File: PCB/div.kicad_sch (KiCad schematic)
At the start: 27 parts, among them J2 Bus Gate Reset, Q4 BC557, U1 4024

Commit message: :hammer: Optimize schematic for PCB layout
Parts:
- D?: value rt -> ye
- J?: footprint Connector_PinHeader_2.54mm:PinHeader_2x08_P2.54mm_Vertical -> Connector_PinHeader_2.54mm:PinHeader_2x08_P2.54mm_Horizontal
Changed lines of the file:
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@@
       (effects (font (size 1.27 1.27)) (justify right))
     )
-    (property "Value" "rt" (at 107.315 36.195 90)
+    (property "Value" "ye" (at 107.315 36.195 90)
       (effects (font (size 1.27 1.27)) (justify right))
     )
@@
   (symbol (lib_id "Connector_Generic:Conn_02x08_Odd_Even") (at 40.64 181.61 180) (unit 1)
     (in_bom yes) (on_board yes) (dnp no) (fields_autoplaced)
-    (property "Reference" "J?" (at 39.37 166.4802 0)
-      (effects (font (size 1.27 1.27)))
-    )
-    (property "Value" "PWR" (at 39.37 169.0171 0)
-      (effects (font (size 1.27 1.27)))
-    )
-    (property "Footprint" "Connector_PinHeader_2.54mm:PinHeader_2x08_P2.54mm_Vertical" (at 40.64 181.61 0)
-      (effects (font (size 1.27 1.27)) hide)
-    )
+    (property "Reference" "J?" (at 39.37 167.1701 0)
+      (effects (font (size 1.27 1.27)))
+    )
+    (property "Value" "PWR" (at 39.37 169.0911 0)
+      (effects (font (size 1.27 1.27)))
+    )
+    (property "Footprint" "Connector_PinHeader_2.54mm:PinHeader_2x08_P2.54mm_Horizontal" (at 40.64 181.61 0)
+      (effects (font (size 1.27 1.27)) hide)
+    )

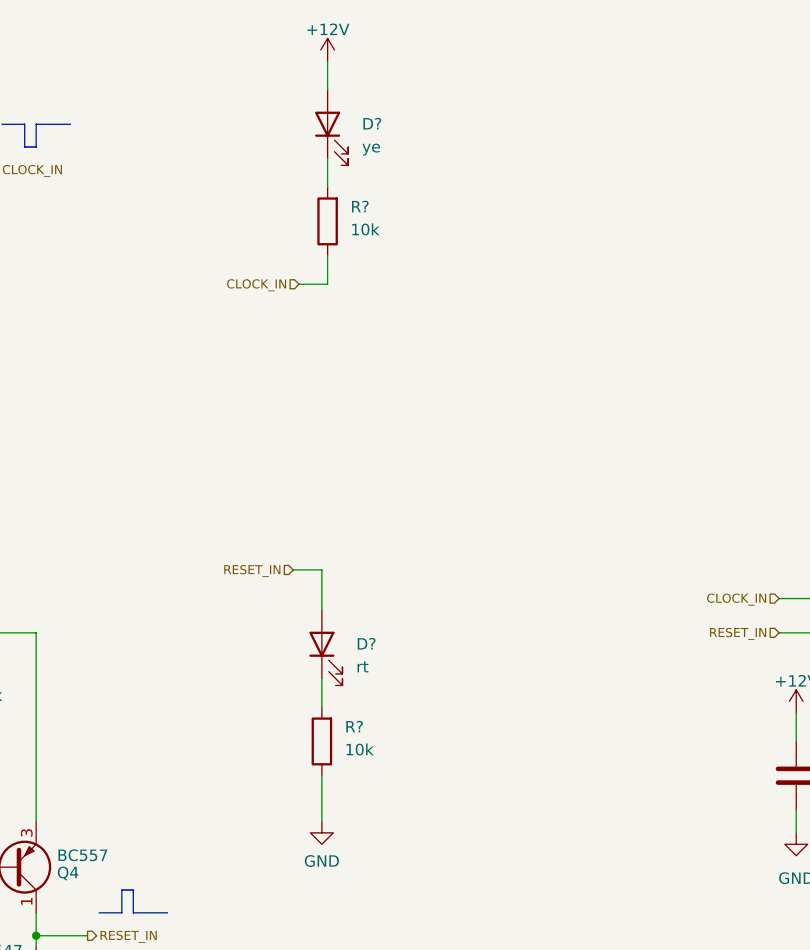
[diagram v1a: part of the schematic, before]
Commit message: :sparkles: Add jack LEDs to the schematic
Using clear jacks the LEDs can be put underneath them. The control
PCB can support both versions (LEDs separate or in jacks), so a
second (SMD) LED is added to the schematic.

Only one of these may be populated!
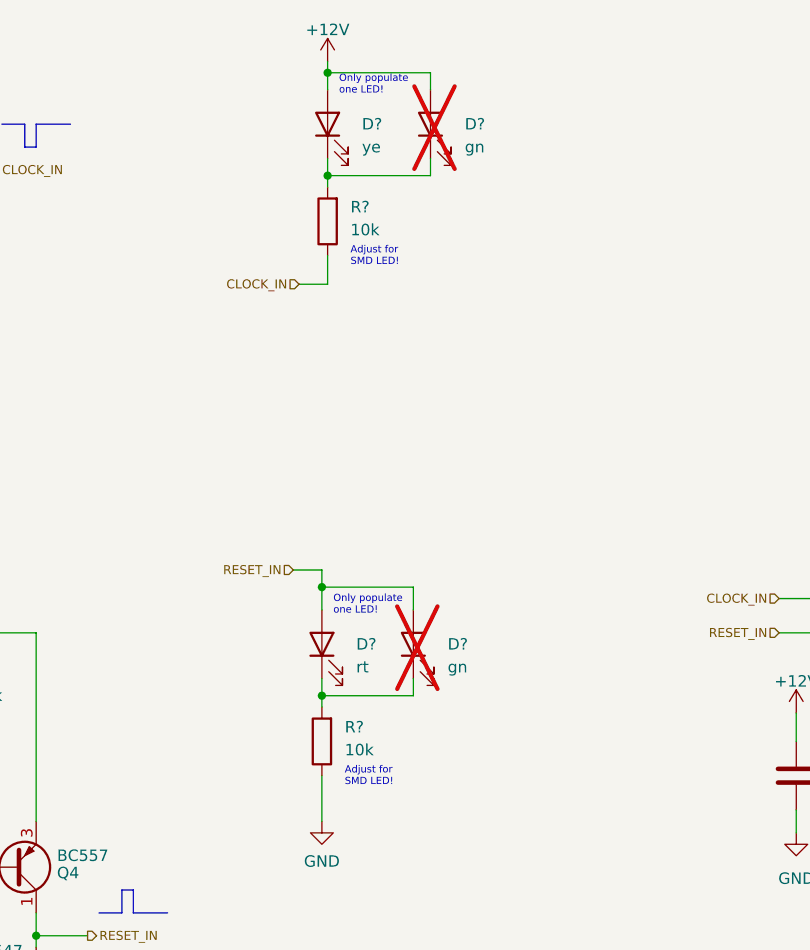
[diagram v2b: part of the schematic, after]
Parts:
- added D? (x2): gn, LED_SMD:LED_0805_2012Metric_Pad1.15x1.40mm_HandSolder, symbol Device:LED
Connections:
- net +12V: now also D?.2 (A)
- net RESET_IN: now also D?.2 (A)
- net at D?.1 (K), R?.2: now also D?.1 (K) (x2)
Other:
- note added: "Adjust for SMD LED!"
- note added: "Only populate one LED!"

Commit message: :hammer: Change power connector footprint in schematic
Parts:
- J?: footprint Connector_PinHeader_2.54mm:PinHeader_2x08_P2.54mm_Horizontal -> Connector_PinHeader_2.54mm:PinHeader_2x08_P2.54mm_Vertical
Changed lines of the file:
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@@
       (effects (font (size 1.27 1.27)))
     )
-    (property "Footprint" "Connector_PinHeader_2.54mm:PinHeader_2x08_P2.54mm_Horizontal" (at 40.64 181.61 0)
+    (property "Footprint" "Connector_PinHeader_2.54mm:PinHeader_2x08_P2.54mm_Vertical" (at 40.64 181.61 0)
       (effects (font (size 1.27 1.27)) hide)
     )

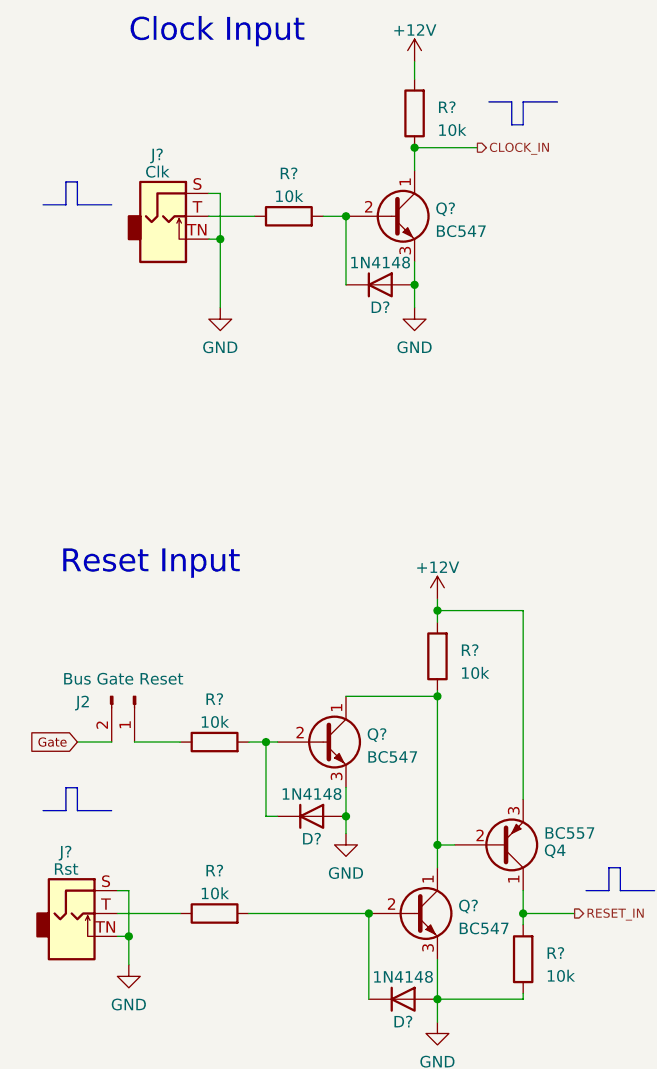
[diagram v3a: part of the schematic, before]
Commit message: :wrench: Increase input resistors to improve impedance
Set the input resistors to 100K to improve input impedance.
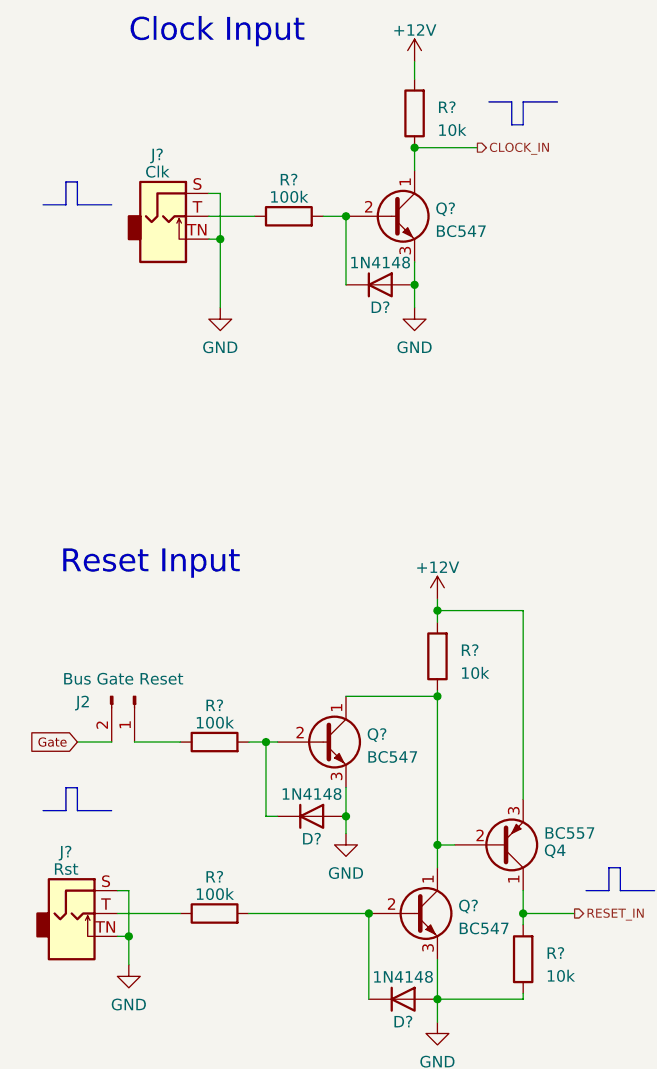
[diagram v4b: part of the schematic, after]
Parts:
- R? (x3): value 10k -> 100k
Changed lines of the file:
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@@
   (symbol (lib_id "Device:R") (at 36.83 104.775 90) (unit 1)
     (in_bom yes) (on_board yes) (dnp no) (fields_autoplaced)
-    (property "Reference" "R?" (at 36.83 100.0592 90)
-      (effects (font (size 1.27 1.27)))
-    )
-    (property "Value" "10k" (at 36.83 102.5961 90)
+    (property "Reference" "R?" (at 36.83 100.7491 90)
+      (effects (font (size 1.27 1.27)))
+    )
+    (property "Value" "100k" (at 36.83 102.6701 90)
       (effects (font (size 1.27 1.27)))
     )
@@
   (symbol (lib_id "Device:R") (at 36.83 123.825 90) (unit 1)
     (in_bom yes) (on_board yes) (dnp no) (fields_autoplaced)
-    (property "Reference" "R?" (at 36.83 119.1092 90)
-      (effects (font (size 1.27 1.27)))
-    )
-    (property "Value" "10k" (at 36.83 121.6461 90)
+    (property "Reference" "R?" (at 36.83 119.7991 90)
+      (effects (font (size 1.27 1.27)))
+    )
+    (property "Value" "100k" (at 36.83 121.7201 90)
       (effects (font (size 1.27 1.27)))
     )
@@
   (symbol (lib_id "Device:R") (at 45.085 46.355 90) (unit 1)
     (in_bom yes) (on_board yes) (dnp no) (fields_autoplaced)
-    (property "Reference" "R?" (at 45.085 41.6392 90)
-      (effects (font (size 1.27 1.27)))
-    )
-    (property "Value" "10k" (at 45.085 44.1761 90)
-      (effects (font (size 1.27 1.27)))
-    )
+    (property "Reference" "R?" (at 45.085 42.3291 90)
+      (effects (font (size 1.27 1.27)))
+    )
+    (property "Value" "100k" (at 45.085 44.2501 90)
+      (effects (font (size 1.27 1.27)))
+    )

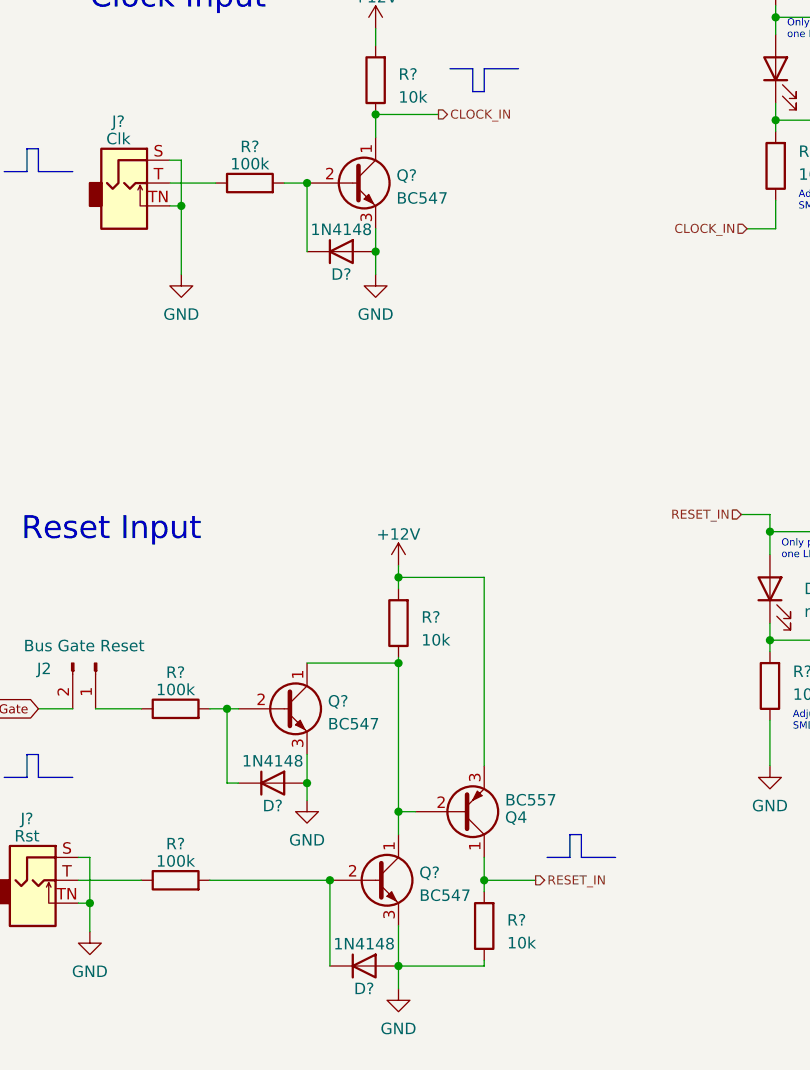
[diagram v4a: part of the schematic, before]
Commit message: :wrench: Change transistor footprint to handsolder version
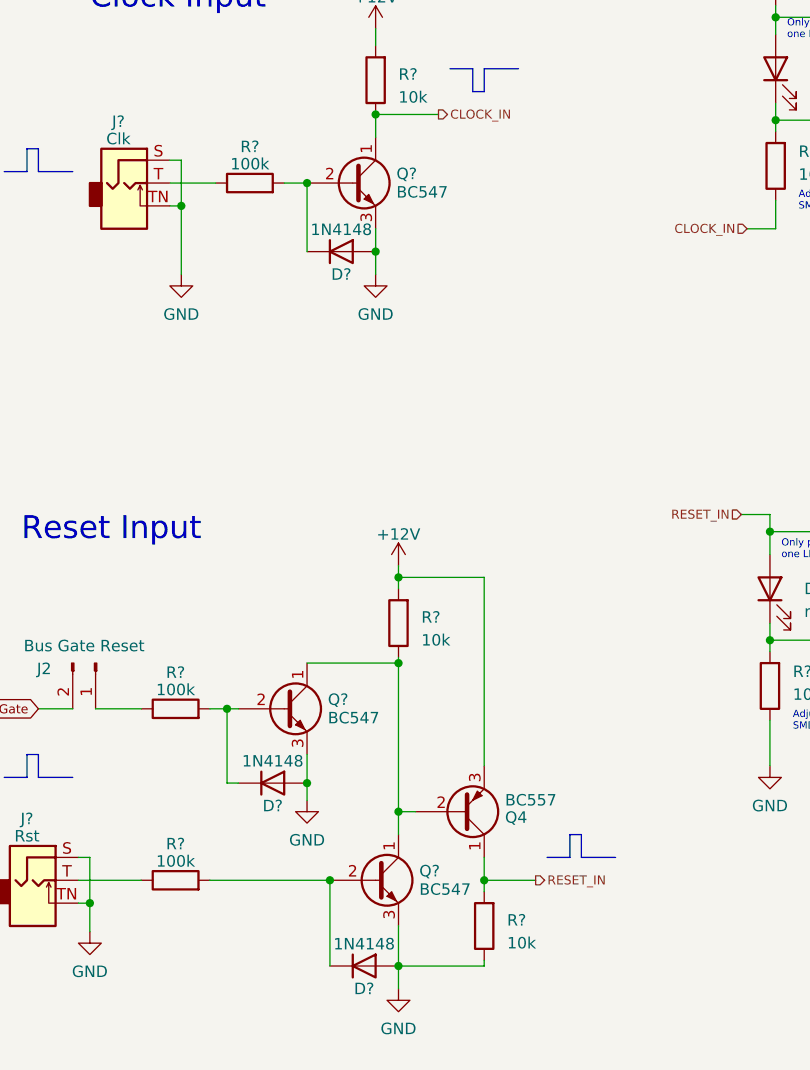
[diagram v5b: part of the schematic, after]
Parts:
- Q4, Q? (x3): footprint Package_TO_SOT_THT:TO-92_Inline -> Package_TO_SOT_THT:TO-92_HandSolder
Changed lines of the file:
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@@
   (symbol (lib_id "Transistor_BJT:BC547") (at 56.515 46.355 0) (unit 1)
     (in_bom yes) (on_board yes) (dnp no) (fields_autoplaced)
-    (property "Reference" "Q?" (at 61.3664 45.5203 0)
-      (effects (font (size 1.27 1.27)) (justify left))
-    )
-    (property "Value" "BC547" (at 61.3664 48.0572 0)
-      (effects (font (size 1.27 1.27)) (justify left))
-    )
-    (property "Footprint" "Package_TO_SOT_THT:TO-92_Inline" (at 61.595 48.26 0)
+    (property "Reference" "Q?" (at 61.3664 45.331 0)
+      (effects (font (size 1.27 1.27)) (justify left))
+    )
+    (property "Value" "BC547" (at 61.3664 47.379 0)
+      (effects (font (size 1.27 1.27)) (justify left))
+    )
+    (property "Footprint" "Package_TO_SOT_THT:TO-92_HandSolder" (at 61.595 48.26 0)
       (effects (font (size 1.27 1.27) italic) (justify left) hide)
     )
@@
       (effects (font (size 1.27 1.27)) (justify left))
     )
-    (property "Footprint" "Package_TO_SOT_THT:TO-92_Inline" (at 73.66 114.3 0)
+    (property "Footprint" "Package_TO_SOT_THT:TO-92_HandSolder" (at 73.66 114.3 0)
       (effects (font (size 1.27 1.27) italic) (justify left) hide)
     )
@@
   (symbol (lib_id "Transistor_BJT:BC547") (at 59.055 123.825 0) (unit 1)
     (in_bom yes) (on_board yes) (dnp no) (fields_autoplaced)
-    (property "Reference" "Q?" (at 63.9064 122.9903 0)
-      (effects (font (size 1.27 1.27)) (justify left))
-    )
-    (property "Value" "BC547" (at 63.9064 125.5272 0)
-      (effects (font (size 1.27 1.27)) (justify left))
-    )
-    (property "Footprint" "Package_TO_SOT_THT:TO-92_Inline" (at 64.135 125.73 0)
+    (property "Reference" "Q?" (at 63.9064 122.801 0)
+      (effects (font (size 1.27 1.27)) (justify left))
+    )
+    (property "Value" "BC547" (at 63.9064 124.849 0)
+      (effects (font (size 1.27 1.27)) (justify left))
+    )
+    (property "Footprint" "Package_TO_SOT_THT:TO-92_HandSolder" (at 64.135 125.73 0)
       (effects (font (size 1.27 1.27) italic) (justify left) hide)
     )
@@
   (symbol (lib_id "Transistor_BJT:BC547") (at 48.895 104.775 0) (unit 1)
     (in_bom yes) (on_board yes) (dnp no) (fields_autoplaced)
-    (property "Reference" "Q?" (at 53.7464 103.9403 0)
-      (effects (font (size 1.27 1.27)) (justify left))
-    )
-    (property "Value" "BC547" (at 53.7464 106.4772 0)
-      (effects (font (size 1.27 1.27)) (justify left))
-    )
-    (property "Footprint" "Package_TO_SOT_THT:TO-92_Inline" (at 53.975 106.68 0)
+    (property "Reference" "Q?" (at 53.7464 103.751 0)
+      (effects (font (size 1.27 1.27)) (justify left))
+    )
+    (property "Value" "BC547" (at 53.7464 105.799 0)
+      (effects (font (size 1.27 1.27)) (justify left))
+    )
+    (property "Footprint" "Package_TO_SOT_THT:TO-92_HandSolder" (at 53.975 106.68 0)
       (effects (font (size 1.27 1.27) italic) (justify left) hide)
     )
